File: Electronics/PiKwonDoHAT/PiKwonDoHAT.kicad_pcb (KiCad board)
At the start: 2 copper layers, 5 parts, among them J1 Conn_02x20_Odd_Even, J2 Judge3, J3 Judge2, J4 Judge1, J5 Controller

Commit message: Finalized HAT PCB design
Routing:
- net /CLK: track 100.8 -> 60.5 mm, vias 6 -> 4
- net GND: track 76.3 -> 72.2 mm
- net Net-(J1-Pad29): track 10.0 -> 12.0 mm
- net Net-(J1-Pad3): track 9.17 -> 8.14 mm
- net /LOAD: track 80.0 -> 79.0 mm
- net Net-(J1-Pad11): track 6.14 -> 7.06 mm
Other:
- board outline added: 24 x 61 mm

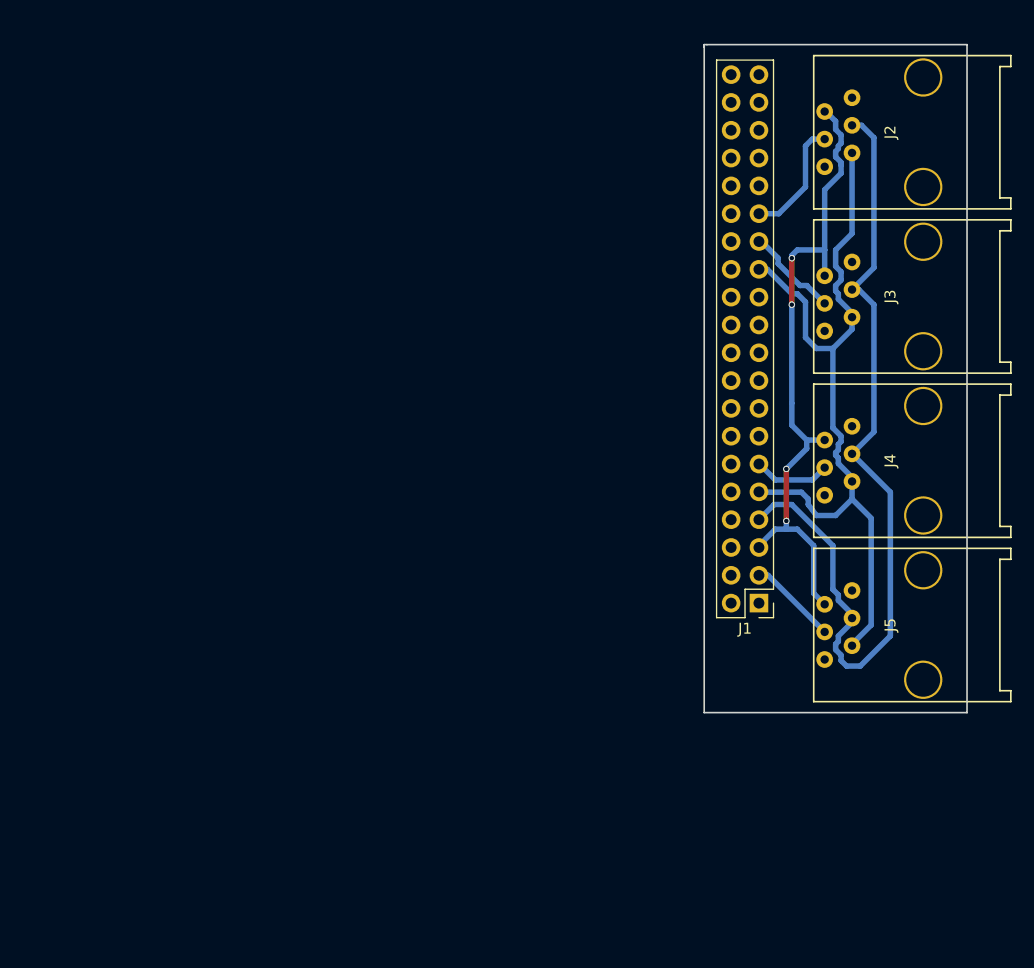
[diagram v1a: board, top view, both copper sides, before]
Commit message: Updated circuit protection elements to HAT schematic board.
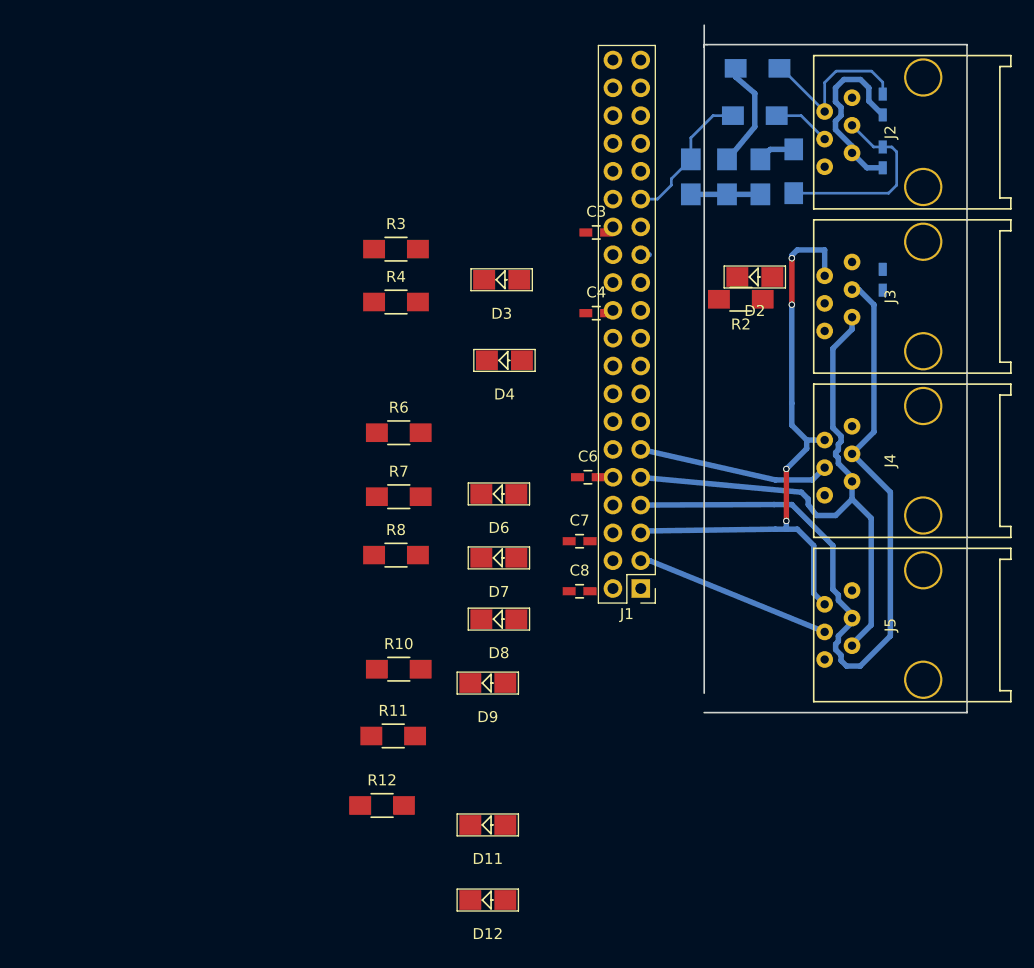
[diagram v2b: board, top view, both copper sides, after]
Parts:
- added C1: 270pF, Capacitors_SMD:C_0603_HandSoldering, B.Cu at (146.3, 82.3)
- added C2: 270pF, Capacitors_SMD:C_0603_HandSoldering, B.Cu at (146.3, 93.5)
- added C3: 270pF, Capacitors_SMD:C_0603_HandSoldering, F.Cu at (120.1, 89.2)
- added C4: 270pF, Capacitors_SMD:C_0603_HandSoldering, F.Cu at (120.1, 96.5)
- added C5: 270pF, Capacitors_SMD:C_0603_HandSoldering, B.Cu at (146.3, 77.5)
- added C6: 270pF, Capacitors_SMD:C_0603_HandSoldering, F.Cu at (119.4, 111.5)
- added C7: 270pF, Capacitors_SMD:C_0603_HandSoldering, F.Cu at (118.6, 117.3)
- added C8: 270pF, Capacitors_SMD:C_0603_HandSoldering, F.Cu at (118.6, 121.9)
- added D1: D_Zener, Diodes_SMD:SOD-80C, B.Cu at (128.8, 84.1)
- added D10: D_Zener, Diodes_SMD:SOD-80C, B.Cu at (132.1, 84.1)
- added D11: D_Zener, Diodes_SMD:SOD-80C, F.Cu at (110.2, 143.3)
- added D12: D_Zener, Diodes_SMD:SOD-80C, F.Cu at (110.2, 150.1)
- added D2: D_Zener, Diodes_SMD:SOD-80C, F.Cu at (134.6, 93.2)
- added D3: D_Zener, Diodes_SMD:SOD-80C, F.Cu at (111.5, 93.5)
- added D4: D_Zener, Diodes_SMD:SOD-80C, F.Cu at (111.8, 100.8)
- added D5: D_Zener, Diodes_SMD:SOD-80C, B.Cu at (135.1, 84.1)
- added D6: D_Zener, Diodes_SMD:SOD-80C, F.Cu at (111.3, 113.0)
- added D7: D_Zener, Diodes_SMD:SOD-80C, F.Cu at (111.3, 118.9)
- added D8: D_Zener, Diodes_SMD:SOD-80C, F.Cu at (111.3, 124.5)
- added D9: D_Zener, Diodes_SMD:SOD-80C, F.Cu at (110.2, 130.3)
- added R1: 470, Resistors_SMD:R_1206_HandSoldering, B.Cu at (134.6, 78.5)
- added R10: 470, Resistors_SMD:R_1206_HandSoldering, F.Cu at (102.1, 129.0)
- added R11: 470, Resistors_SMD:R_1206_HandSoldering, F.Cu at (101.6, 135.1)
- added R12: 470, Resistors_SMD:R_1206_HandSoldering, F.Cu at (100.6, 141.5)
- added R2: 470, Resistors_SMD:R_1206_HandSoldering, F.Cu at (133.3, 95.2)
- added R3: 470, Resistors_SMD:R_1206_HandSoldering, F.Cu at (101.9, 90.7)
- added R4: 470, Resistors_SMD:R_1206_HandSoldering, F.Cu at (101.9, 95.5)
- added R5: 470, Resistors_SMD:R_1206_HandSoldering, B.Cu at (138.2, 83.6)
- added R6: 470, Resistors_SMD:R_1206_HandSoldering, F.Cu at (102.1, 107.4)
- added R7: 470, Resistors_SMD:R_1206_HandSoldering, F.Cu at (102.1, 113.3)
- added R8: 470, Resistors_SMD:R_1206_HandSoldering, F.Cu at (101.9, 118.6)
- added R9: 470, Resistors_SMD:R_1206_HandSoldering, B.Cu at (134.9, 74.2)
- moved J1 10.9 mm to (124.2, 121.7)
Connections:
- J1 pad 11: Net-(J1-Pad11) -> Net-(D3-Pad1)
- J1 pad 27: Net-(J1-Pad27) -> Net-(D2-Pad1)
- J1 pad 29: Net-(J1-Pad29) -> Net-(D1-Pad1)
- J1 pad 3: Net-(J1-Pad3) -> Net-(D4-Pad1)
- J2 pad 2: /CLK -> Net-(C5-Pad1)
- J2 pad 3: /LOAD -> Net-(C1-Pad1)
- J2 pad 4: Net-(J1-Pad29) -> Net-(J2-Pad4)
- J3 pad 2: /CLK -> Net-(C6-Pad1)
- J3 pad 3: /LOAD -> Net-(C2-Pad1)
- J3 pad 4: Net-(J1-Pad27) -> Net-(J3-Pad4)
- J4 pad 2: /CLK -> Net-(C7-Pad1)
- J4 pad 3: /LOAD -> Net-(C3-Pad1)
- J4 pad 4: Net-(J1-Pad11) -> Net-(J4-Pad4)
- J5 pad 2: /CLK -> Net-(C8-Pad1)
- J5 pad 3: /LOAD -> Net-(C4-Pad1)
- J5 pad 4: Net-(J1-Pad3) -> Net-(J5-Pad4)
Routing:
- net /LOAD: track 79.0 -> 27.7 mm
- net Net-(C3-Pad1): track 0.00 -> 29.3 mm
- net Net-(D4-Pad1): track 0.00 -> 18.1 mm
- net Net-(C1-Pad1): track 0.00 -> 17.8 mm
- net Net-(C5-Pad1): track 0.00 -> 16.1 mm
- net Net-(D3-Pad1): track 0.00 -> 16.0 mm
- net Net-(C2-Pad1): track 0.00 -> 14.2 mm
- net Net-(D1-Pad1): track 0.00 -> 13.1 mm
- net Net-(J1-Pad29): track 12.0 -> 0.00 mm
- net Net-(J1-Pad27): track 9.02 -> 0.00 mm
- net Net-(J1-Pad3): track 8.14 -> 0.00 mm
- net GND: track 72.2 -> 79.3 mm
- net Net-(J1-Pad11): track 7.06 -> 0.00 mm
- net Net-(J2-Pad4): track 0.00 -> 6.28 mm
- net Net-(C4-Pad1): track 0.00 -> 4.29 mm
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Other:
- board size 24 x 61 mm -> 24 x 62.8 mm

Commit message: Updated CAM files for Timer and PCB for HAT
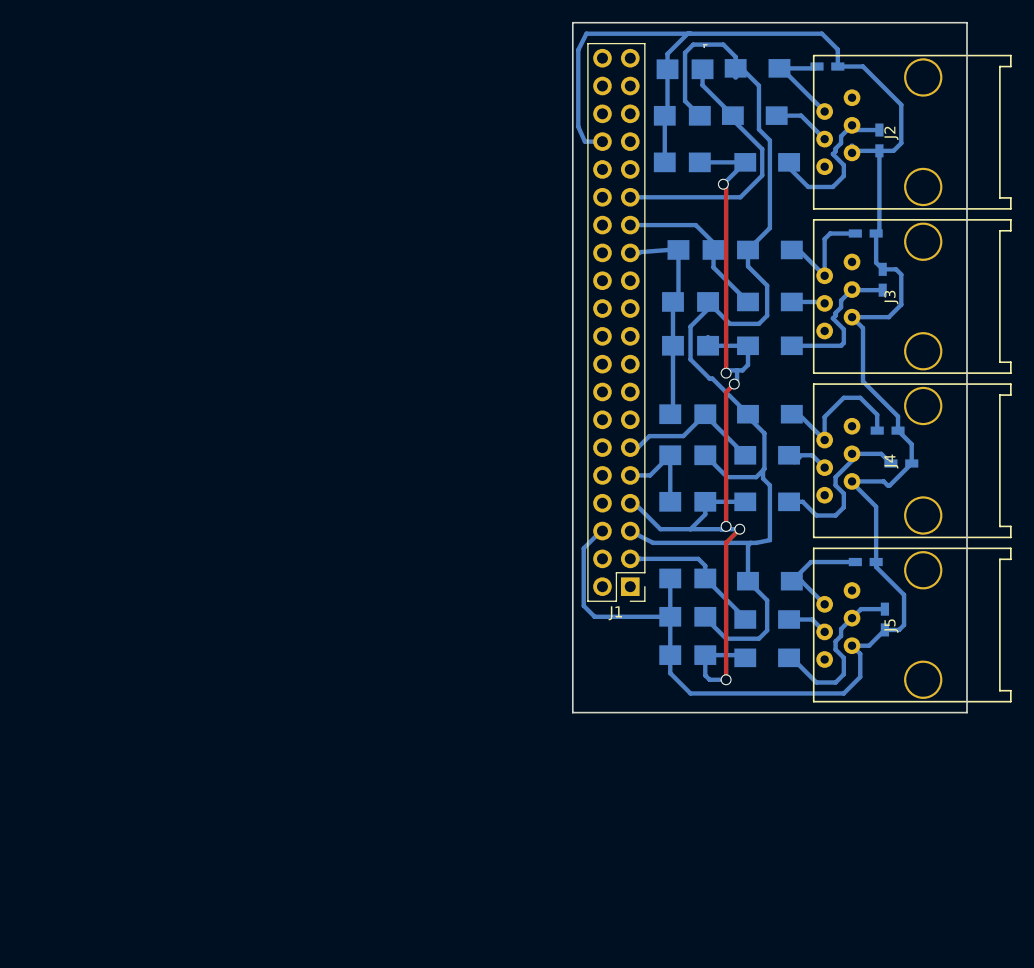
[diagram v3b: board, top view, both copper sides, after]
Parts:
- C3, C4, C6, C7, C8, D11, D12, D2, D3, D4, D6, D7, D8, D9, R10, R11, R12, R2, R3, R4, R6, R7, R8: moved to B.Cu
- moved D9 54.8 mm to (128.0, 78.5), turned to 180 degrees
- moved R10 51.1 mm to (136.0, 90.8), turned to 180 degrees
- moved R11 45.2 mm to (136.0, 105.8), turned to 180 degrees
- moved R4 44.6 mm to (135.8, 124.5), turned to 180 degrees
- moved R12 40.9 mm to (136.0, 121.0), turned to 180 degrees
- moved R3 38.8 mm to (135.8, 109.5), turned to 180 degrees
- moved C4 38.4 mm to (146.5, 124.5), turned to 270 degrees
- moved D11 38.4 mm to (128.5, 109.5), turned to 180 degrees
- moved R8 35.2 mm to (135.8, 128.0), turned to 180 degrees
- moved C3 34.9 mm to (148.0, 110.2)
- moved R6 34.8 mm to (136.0, 99.5), turned to 180 degrees
- moved C6 33.7 mm to (144.8, 89.2)
- moved R7 33.6 mm to (135.8, 113.8), turned to 180 degrees
- moved D12 31.7 mm to (128.5, 124.2), turned to 180 degrees
- moved C7 29.9 mm to (146.8, 107.2)
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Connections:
- J1 pad 34: (no net) -> GND
- J1 pad 6: (no net) -> GND
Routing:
- net GND: track 79.3 -> 208.3 mm
- net /LOAD: track 27.7 -> 87.7 mm, vias 0 -> 6
- net /CLK: track 60.6 -> 107.7 mm, vias 4 -> 0
- net Net-(D2-Pad1): track 0.25 -> 15.2 mm
- net Net-(C3-Pad1): track 29.3 -> 15.6 mm
- net Net-(D1-Pad1): track 13.1 -> 25.4 mm
- net Net-(C4-Pad1): track 4.29 -> 16.4 mm
- net Net-(C7-Pad1): track 1.64 -> 13.7 mm
- net Net-(C8-Pad1): track 1.41 -> 10.4 mm
- net Net-(C6-Pad1): track 2.36 -> 10.3 mm
- net Net-(C5-Pad1): track 16.1 -> 9.75 mm
- net Net-(J5-Pad4): track 0.00 -> 3.72 mm
- net Net-(D4-Pad1): track 18.1 -> 14.4 mm
- net Net-(J3-Pad4): track 0.37 -> 3.42 mm
- net Net-(J4-Pad4): track 1.58 -> 4.43 mm
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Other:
- board size 24 x 62.8 mm -> 36 x 63 mm
- net class Default: clearance 0.2 -> 0.3; trace_width 0.25 -> 0.4; via_dia 0.6 -> 1; via_drill 0.4 -> 0.8
- net class Routing removed
- rule trace_clearance: 0.2 -> 0.3

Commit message: Finalized HAT PCB
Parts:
- moved C7 5.19 mm to (142.3, 104.5)
- moved R9 1.84 mm to (135.0, 76.0)
- moved D1 1.77 mm to (128.0, 76.0)
- moved C3 1.67 mm to (146.4, 110.6), turned to 270 degrees
- moved R1 1.56 mm to (135.0, 80.0)
- moved D9 1.50 mm to (128.0, 80.0)
- moved R5 1.46 mm to (135.0, 84.0)
- moved D8 1.35 mm to (128.0, 129.0)
- moved D2 1.27 mm to (128.0, 91.0)
- moved D5 1.25 mm to (128.0, 84.0)
- moved R8 1.25 mm to (135.0, 129.0)
- moved R2 1.12 mm to (135.0, 95.0)
- moved R6 1.12 mm to (135.0, 99.0)
- moved R10 1.03 mm to (135.0, 91.0)
- moved R11 1.03 mm to (135.0, 106.0)
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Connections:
- J1 pad 7: /LOAD -> (no net)
- J1 pad 8: (no net) -> /LOAD
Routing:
- net GND: track 208.3 -> 172.7 mm
- net /LOAD: track 87.7 -> 101.0 mm, vias 6 -> 2
- net /CLK: track 107.7 -> 100.3 mm
- net Net-(D1-Pad1): track 25.4 -> 19.5 mm
- net Net-(C5-Pad1): track 9.75 -> 5.42 mm
- net Net-(C7-Pad1): track 13.7 -> 9.84 mm
- net Net-(D3-Pad1): track 13.4 -> 17.3 mm
- net Net-(D2-Pad1): track 15.2 -> 13.5 mm
- net Net-(J3-Pad4): track 3.42 -> 4.81 mm
- net Net-(C2-Pad1): track 14.3 -> 15.4 mm
- net Net-(J2-Pad4): track 6.28 -> 5.27 mm
- net Net-(C4-Pad1): track 16.4 -> 15.5 mm
- net Net-(C6-Pad1): track 10.3 -> 11.2 mm
- net Net-(J5-Pad4): track 3.72 -> 4.26 mm

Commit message: Updated BOM and CAM files for HAT PCB
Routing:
- net GND: track 172.7 -> 180.4 mm
- net Net-(C5-Pad1): track 5.42 -> 9.82 mm
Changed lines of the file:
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@@
-(kicad_pcb (version 4) (host pcbnew 4.0.7)
+(kicad_pcb (version 4) (host pcbnew 4.0.7-e2-6376~61~ubuntu18.04.1)
   (general
     (links 71)
-    (no_connects 5)
-    (area 117.924999 69.924999 154.075001 133.075001)
+    (no_connects 3)
+    (area 113.227618 69.835 158.375001 133.275)
     (thickness 1.6)
     (drawings 6)
-    (tracks 265)
+    (tracks 269)
     (zones 0)
     (modules 37)
@@
     (visible_elements FFFFFF7F)
     (pcbplotparams
-      (layerselection 0x00000_80000000)
+      (layerselection 0x01000_80000000)
       (usegerberextensions false)
       (excludeedgelayer true)
@@
       (viasonmask false)
       (mode 1)
-      (useauxorigin false)
+      (useauxorigin true)
       (hpglpennumber 1)
       (hpglpenspeed 20)
@@
   (segment (start 134 105.75) (end 134 106) (width 0.4) (layer B.Cu) (net 1))
   (segment (start 123.25 116.42) (end 123.25 116.25) (width 0.5) (layer B.Cu) (net 1) (status 30))
-  (segment (start 133 84) (end 133 85.92) (width 0.4) (layer B.Cu) (net 2) (status 400000))
-  (segment (start 133 99.89) (end 133 99) (width 0.4) (layer B.Cu) (net 2) (status 800000))
+  (segment (start 133 84) (end 133 85.92) (width 0.4) (layer B.Cu) (net 2))
+  (segment (start 133 99.89) (end 133 99) (width 0.4) (layer B.Cu) (net 2))
   (segment (start 131.14 101.75) (end 133 99.89) (width 0.4) (layer B.Cu) (net 2))
   (via (at 131.14 101.75) (size 1) (drill 0.8) (layers F.Cu B.Cu) (net 2))
@@
   (via (at 131.14 87.78) (size 1) (drill 0.8) (layers F.Cu B.Cu) (net 2))
   (segment (start 133 85.92) (end 131.14 87.78) (width 0.4) (layer B.Cu) (net 2))
-  (segment (start 129.6 129) (end 129.6 129.452) (width 0.4) (layer B.Cu) (net 2) (status C00000))
-  (segment (start 129.6 129.452) (end 128.346 130.706) (width 0.4) (layer B.Cu) (net 2) (status 400000))
-  (segment (start 118.186 116.404) (end 120.71 113.88) (width 0.4) (layer B.Cu) (net 2) (status 800000))
+  (segment (start 129.6 129) (end 129.6 129.452) (width 0.4) (layer B.Cu) (net 2))
+  (segment (start 129.6 129.452) (end 128.346 130.706) (width 0.4) (layer B.Cu) (net 2))
+  (segment (start 118.186 116.404) (end 120.71 113.88) (width 0.4) (layer B.Cu) (net 2))
   (segment (start 118.186 123.848) (end 118.186 116.404) (width 0.4) (layer B.Cu) (net 2))
   (segment (start 125.044 130.706) (end 118.186 123.848) (width 0.4) (layer B.Cu) (net 2))
@@
   (segment (start 130.1 114.9) (end 130.1 113.75) (width 0.4) (layer B.Cu) (net 2))
   (segment (start 130.35 99.5) (end 130.35 98.7) (width 0.4) (layer B.Cu) (net 2))
+  (segment (start 143.5 96.889) (end 143.5 104.31) (width 0.4) (layer B.Cu) (net 3) (status C00000))
+  (segment (start 143.5 104.31) (end 143.266 104.544) (width 0.4) (layer B.Cu) (net 3) (status C00000))
   (segment (start 126.4 129) (end 126.4 125) (width 0.4) (layer B.Cu) (net 3))
   (segment (start 126.4 125) (end 126.4 121) (width 0.4) (layer B.Cu) (net 3))
@@
   (segment (start 143.5 124.37) (end 143.5 124.75) (width 0.5) (layer B.Cu) (net 7))
   (segment (start 143.5 124.37) (end 143.5 124) (width 0.5) (layer B.Cu) (net 7))
+  (segment (start 140.3 74) (end 140.3 77.41) (width 0.4) (layer B.Cu) (net 8) (status 400000))
+  (segment (start 140.3 77.41) (end 141 78.11) (width 0.4) (layer B.Cu) (net 8) (status 800000))
   (segment (start 137 76) (end 137 75.062) (width 0.4) (layer B.Cu) (net 8))
   (segment (start 138.062 74) (end 140.3 74) (width 0.4) (layer B.Cu) (net 8))
